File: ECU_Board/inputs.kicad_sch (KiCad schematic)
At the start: 31 parts, among them J3 MAP_Connector, U3 SP720

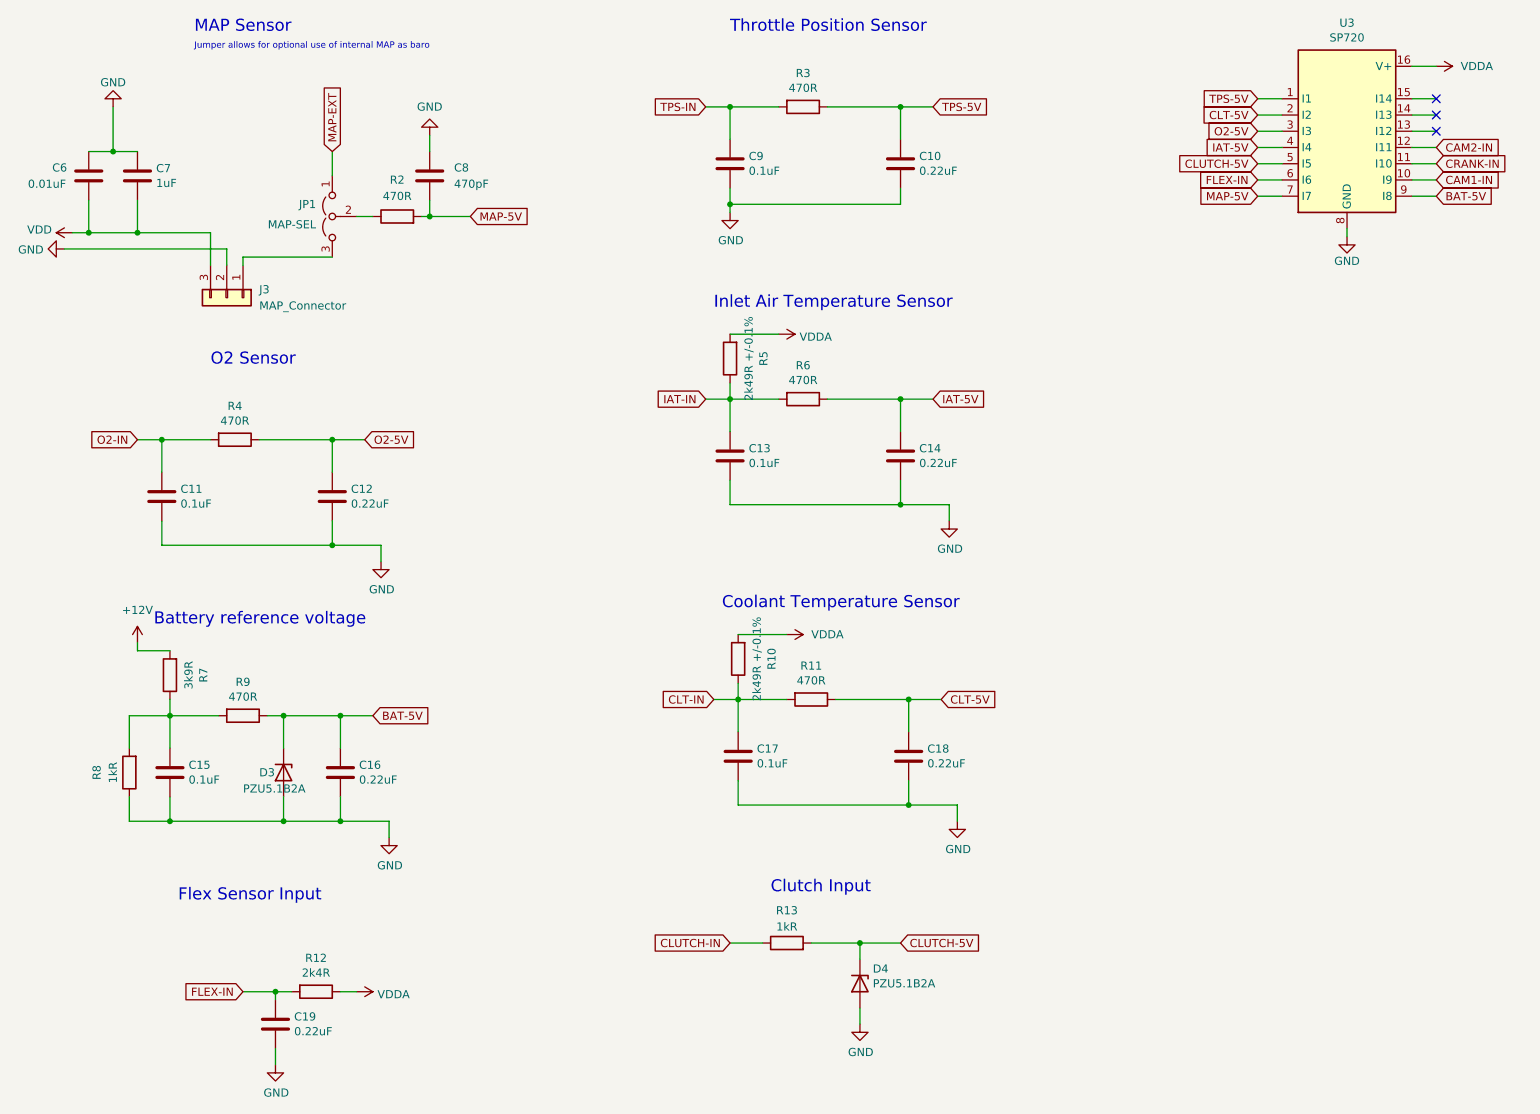
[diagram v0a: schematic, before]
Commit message: Removed clutch input
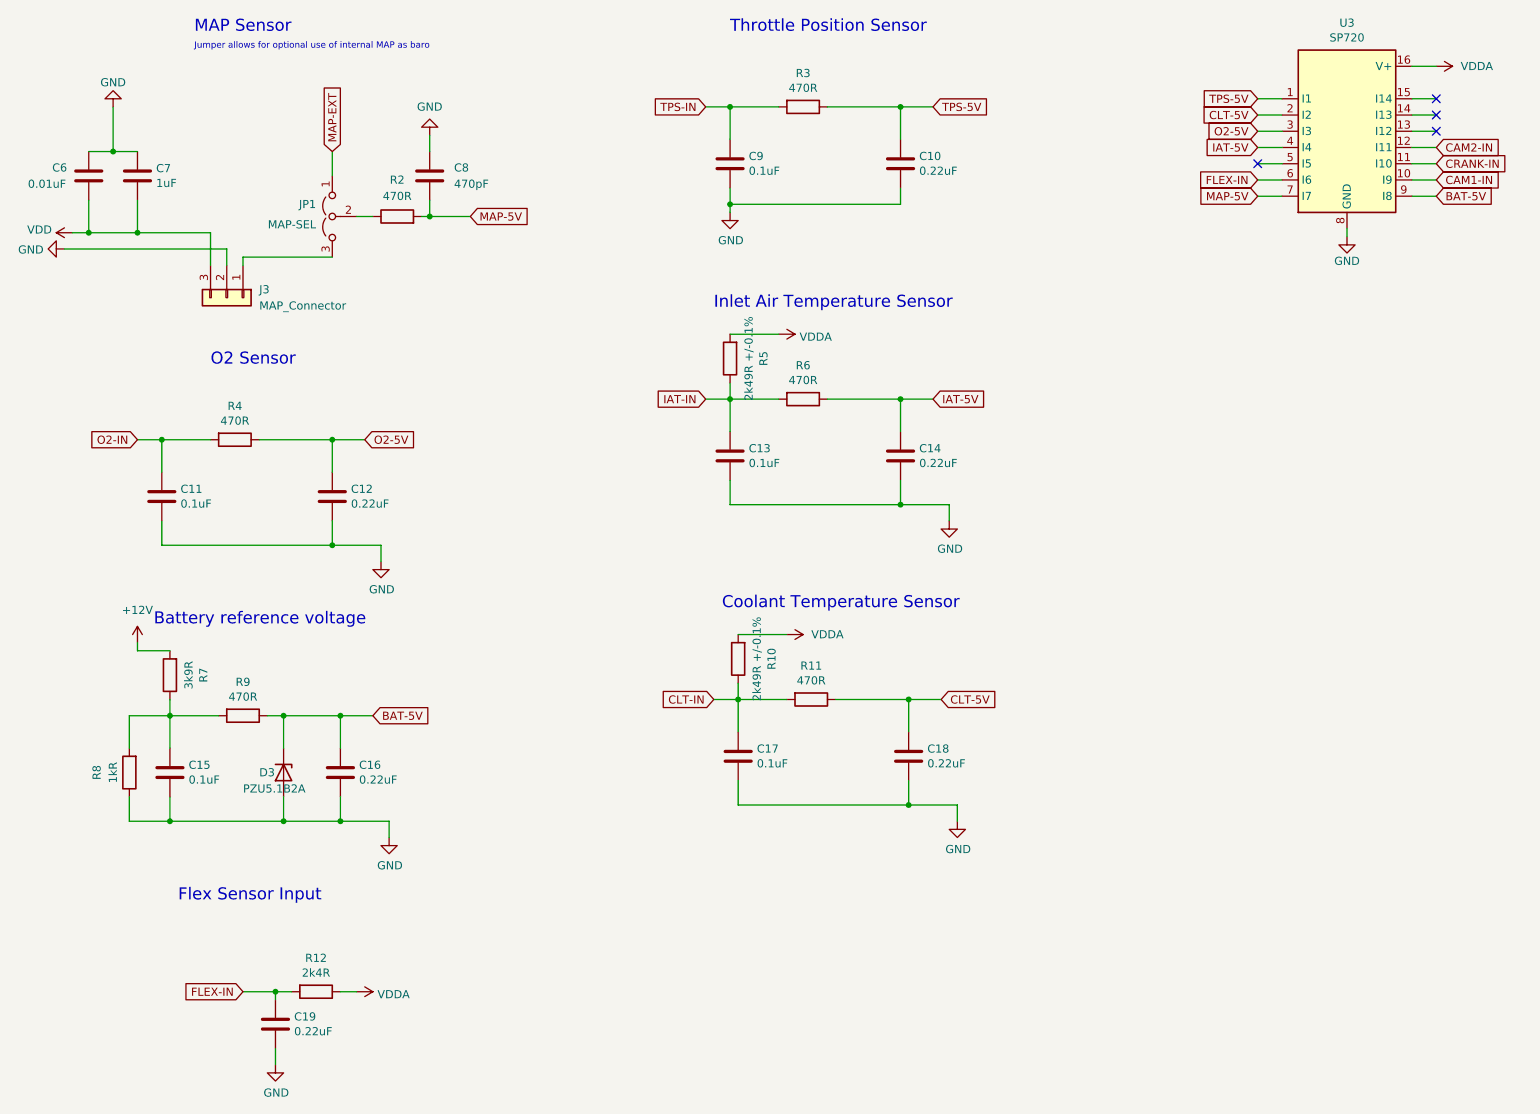
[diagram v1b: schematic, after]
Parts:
- removed D4: PZU5.1B2A, Diode_SMD:D_SOD-323, symbol Device:D_Zener
- removed R13: 1kR, Resistor_SMD:R_0402_1005Metric, symbol Device:R
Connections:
- net CLUTCH-5V: no longer names the net of U3.5 (I5)
- no-connect marks 3 -> 4
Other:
- note removed: "Clutch Input"
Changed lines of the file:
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@@
   (title_block
     (title "Speeduino board for Teensy 4.1")
-    (date "2023-01-02")
-    (rev "5")
+    (date "2023-01-07")
+    (rev "6")
     (company "Fontys Eindhoven EXPO group 13 || Speeduino")
     (comment 1 "Adapted from Speeduino V0.4.4c board")
@@
   )
   (junction (at 130.81 125.73) (diameter 0) (color 0 0 0 0)
-  )
-  (junction (at 149.86 163.83) (diameter 0) (color 0 0 0 0)
   )
   (junction (at 40.64 85.09) (diameter 0) (color 0 0 0 0)
@@
   (no_connect (at 240.03 31.75))
   (no_connect (at 240.03 36.83))
+  (no_connect (at 212.09 41.91))
   (wire (pts (xy 40.64 101.6) (xy 67.31 101.6))
     (stroke (width 0) (type default) (color 0 0 0 0))
@@
     (stroke (width 0) (type default) (color 0 0 0 0))
   )
-  (wire (pts (xy 149.86 166.37) (xy 149.86 163.83))
-    (stroke (width 0) (type default) (color 0 0 0 0))
-  )
   (wire (pts (xy 129.54 83.82) (xy 129.54 78.74))
     (stroke (width 0) (type default) (color 0 0 0 0))
@@
     (stroke (width 0) (type default) (color 0 0 0 0))
   )
-  (wire (pts (xy 129.54 163.83) (xy 134.62 163.83))
-    (stroke (width 0) (type default) (color 0 0 0 0))
-  )
   (wire (pts (xy 41.91 133.35) (xy 41.91 128.27))
     (stroke (width 0) (type default) (color 0 0 0 0))
@@
     (stroke (width 0) (type default) (color 0 0 0 0))
   )
-  (wire (pts (xy 142.24 163.83) (xy 149.86 163.83))
-    (stroke (width 0) (type default) (color 0 0 0 0))
-  )
   (wire (pts (xy 165.1 142.24) (xy 165.1 144.78))
     (stroke (width 0) (type default) (color 0 0 0 0))
@@
     (stroke (width 0) (type default) (color 0 0 0 0))
   )
-  (wire (pts (xy 149.86 163.83) (xy 156.21 163.83))
-    (stroke (width 0) (type default) (color 0 0 0 0))
-  )
   (wire (pts (xy 130.81 123.19) (xy 130.81 125.73))
     (stroke (width 0) (type default) (color 0 0 0 0))
@@
   )
   (wire (pts (xy 156.21 95.25) (xy 163.83 95.25))
-    (stroke (width 0) (type default) (color 0 0 0 0))
-  )
-  (wire (pts (xy 149.86 176.53) (xy 149.86 173.99))
     (stroke (width 0) (type default) (color 0 0 0 0))
   )
@@
   )
   (text "Battery reference voltage" (at 39.37 114.3 0)
-    (effects (font (size 1.8796 1.8796)) (justify left bottom))
-  )
-  (text "Clutch Input" (at 135.89 156.21 0)
     (effects (font (size 1.8796 1.8796)) (justify left bottom))
   )
@@
     )
   )
-  (global_label "CLUTCH-5V" (shape input) (at 156.21 163.83 0) (fields_autoplaced)
-    (effects (font (size 1.27 1.27)) (justify left))
-    (property "Intersheet References" "${INTERSHEET_REFS}" (id 0) (at 169.6902 163.7506 0)
-      (effects (font (size 1.27 1.27)) (justify left) hide)
-    )
-  )
   (global_label "IAT-5V" (shape input) (at 161.29 78.74 0) (fields_autoplaced)
     (effects (font (size 1.27 1.27)) (justify left))
@@
     )
   )
-  (global_label "CLUTCH-IN" (shape input) (at 129.54 163.83 180) (fields_autoplaced)
-    (effects (font (size 1.27 1.27)) (justify right))
-    (property "Intersheet References" "${INTERSHEET_REFS}" (id 0) (at 116.4226 163.7506 0)
-      (effects (font (size 1.27 1.27)) (justify right) hide)
-    )
-  )
   (global_label "MAP-EXT" (shape input) (at 67.31 40.005 90) (fields_autoplaced)
     (effects (font (size 1.27 1.27)) (justify left))
@@
     (effects (font (size 1.27 1.27)) (justify right))
     (property "Intersheet References" "${INTERSHEET_REFS}" (id 0) (at 203.1455 39.2906 0)
-      (effects (font (size 1.27 1.27)) (justify right) hide)
-    )
-  )
-  (global_label "CLUTCH-5V" (shape input) (at 212.09 41.91 180) (fields_autoplaced)
-    (effects (font (size 1.27 1.27)) (justify right))
-    (property "Intersheet References" "${INTERSHEET_REFS}" (id 0) (at 198.6098 41.9894 0)
       (effects (font (size 1.27 1.27)) (justify right) hide)
     )
@@
     (pin "2")
   )
-  (symbol (lib_id "Device:R") (at 138.43 163.83 90) (unit 1)
-    (in_bom yes) (on_board yes)
-    (property "Reference" "R13" (id 0) (at 138.43 158.75 90))
-    (property "Value" "1kR" (id 1) (at 138.43 161.29 90))
-    (property "Footprint" "Resistor_SMD:R_0402_1005Metric" (id 2) (at 138.43 165.608 90)
-      (effects (font (size 1.27 1.27)) hide)
-    )
-    (property "Datasheet" "~" (id 3) (at 138.43 163.83 0)
-      (effects (font (size 1.27 1.27)) hide)
-    )
-    (property "Digikey Part Number" "2502798" (id 4) (at 302.26 302.26 0)
-      (effects (font (size 1.27 1.27)) hide)
-    )
-    (property "Manufacturer_Name" "Walsin" (id 5) (at 302.26 302.26 0)
-      (effects (font (size 1.27 1.27)) hide)
-    )
-    (property "Manufacturer_Part_Number" "WF04P1001FTL" (id 6) (at 302.26 302.26 0)
-      (effects (font (size 1.27 1.27)) hide)
-    )
-    (property "URL" "https://nl.farnell.com/walsin/wf04p1001ftl/res-1k-1-50v-0402-thick-film/dp/2502798" (id 7) (at 302.26 302.26 0)
-      (effects (font (size 1.27 1.27)) hide)
-    )
-    (pin "1")
-    (pin "2")
-  )
-  (symbol (lib_id "Device:D_Zener") (at 149.86 170.18 270) (unit 1)
-    (in_bom yes) (on_board yes)
-    (property "Reference" "D4" (id 0) (at 151.8666 167.8686 90)
-      (effects (font (size 1.27 1.27)) (justify left))
-    )
-    (property "Value" "PZU5.1B2A" (id 1) (at 151.8666 170.18 90)
-      (effects (font (size 1.27 1.27)) (justify left))
-    )
-    (property "Footprint" "Diode_SMD:D_SOD-323" (id 2) (at 149.86 170.18 0)
-      (effects (font (size 1.27 1.27)) hide)
-    )
-    (property "Datasheet" "~" (id 3) (at 149.86 170.18 0)
-      (effects (font (size 1.27 1.27)) hide)
-    )
-    (property "Digikey Part Number" "4126444" (id 5) (at -20.32 20.32 0)
-      (effects (font (size 1.27 1.27)) hide)
-    )
-    (property "Manufacturer_Name" "Nexperia" (id 6) (at -20.32 20.32 0)
-      (effects (font (size 1.27 1.27)) hide)
-    )
-    (property "Manufacturer_Part_Number" "PZU5.1B2A-QX" (id 7) (at -20.32 20.32 0)
-      (effects (font (size 1.27 1.27)) hide)
-    )
-    (property "URL" "https://nl.farnell.com/nexperia/pzu5-1b2a-qx/zener-diode-5-1v-0-49w-sod-323/dp/4126444" (id 8) (at -20.32 20.32 0)
-      (effects (font (size 1.27 1.27)) hide)
-    )
-    (pin "1")
-    (pin "2")
-  )
-  (symbol (lib_id "power:GND") (at 149.86 176.53 0) (unit 1)
-    (in_bom yes) (on_board yes)
-    (property "Reference" "#PWR0142" (id 0) (at 149.86 182.88 0)
-      (effects (font (size 1.27 1.27)) hide)
-    )
-    (property "Value" "GND" (id 1) (at 149.987 180.9242 0))
-    (property "Footprint" "" (id 2) (at 149.86 176.53 0)
-      (effects (font (size 1.27 1.27)) hide)
-    )
-    (property "Datasheet" "" (id 3) (at 149.86 176.53 0)
-      (effects (font (size 1.27 1.27)) hide)
-    )
-    (pin "1")
-  )
   (symbol (lib_id "Device:R") (at 64.77 171.45 270) (unit 1)
